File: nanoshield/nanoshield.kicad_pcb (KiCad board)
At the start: 2 copper layers, 73.7 x 55.9 mm, 8 parts, among them J1 Conn_01x20_Socket, J2 Joy, J3 Conn_01x20_Socket, J4 M0S, J5 DIN-5_180degree

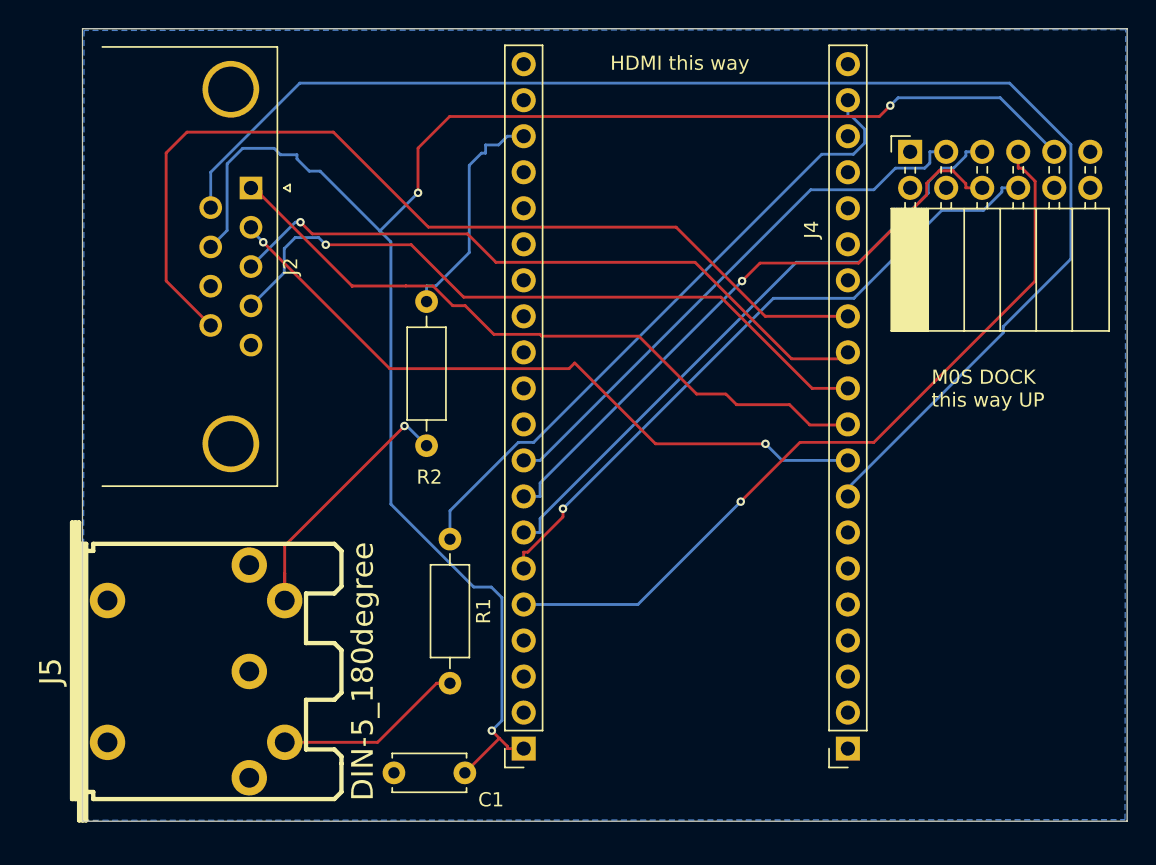
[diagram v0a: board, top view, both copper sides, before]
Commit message: relocation of some components
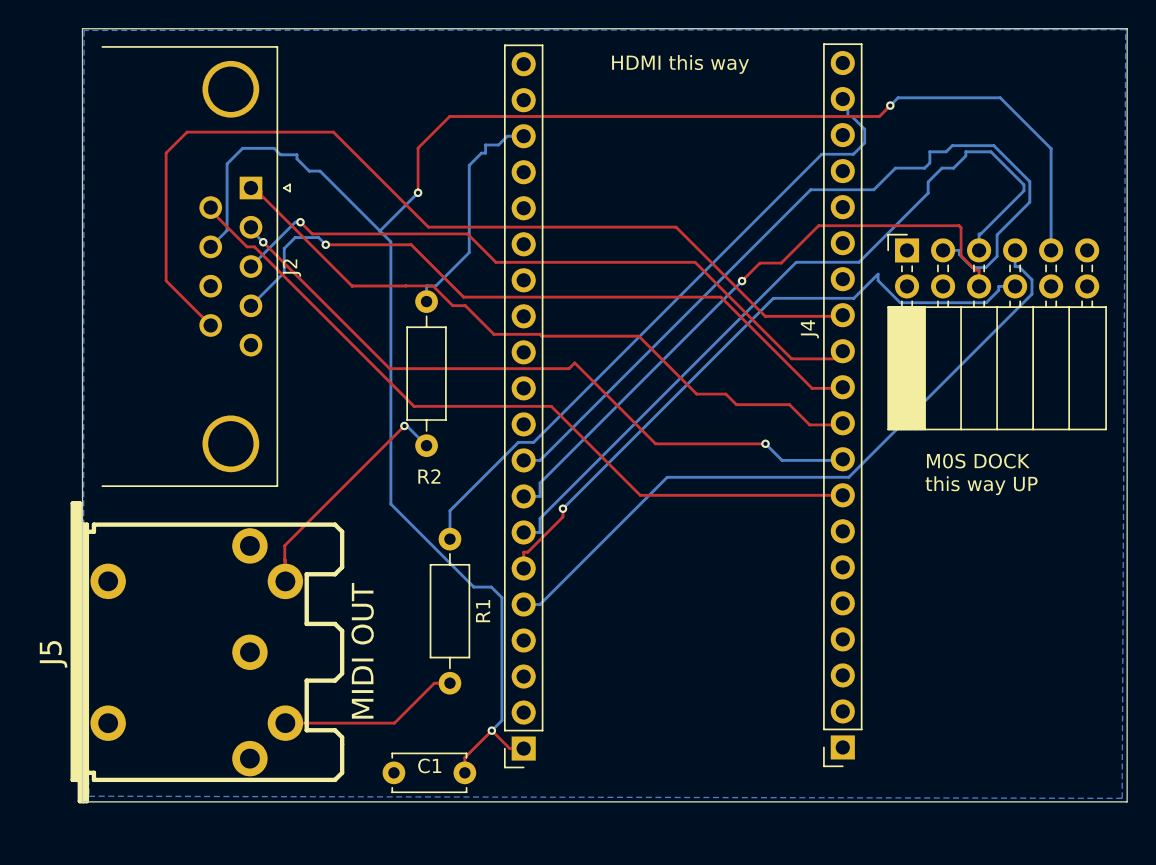
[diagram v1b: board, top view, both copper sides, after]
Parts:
- J5: value DIN-5_180degree -> MIDI OUT
- moved J4 6.95 mm to (149.6, 46.1)
- moved J5 1.35 mm to (100.2, 74.4)
- moved J1 0.37 mm to (145.1, 81.2)
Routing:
- net btn0: track 98.7 -> 52.9 mm
- net irq: track 39.3 -> 57.4 mm
- net csn: track 44.7 -> 54.6 mm
- net +5V: track 121.2 -> 128.2 mm
- net miso: track 55.3 -> 48.6 mm, vias 1 -> 0
- net Net-(J5-Pad5): track 19.1 -> 16.0 mm
- net mosi: track 47.2 -> 46.0 mm
- net left: track 46.9 -> 47.7 mm
- net sck: track 43.5 -> 44.2 mm
- net Net-(J5-Pad4): track 13.4 -> 12.8 mm
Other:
- board size 73.7 x 55.9 mm -> 73.7 x 54.5 mm

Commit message: fix M0S dock location
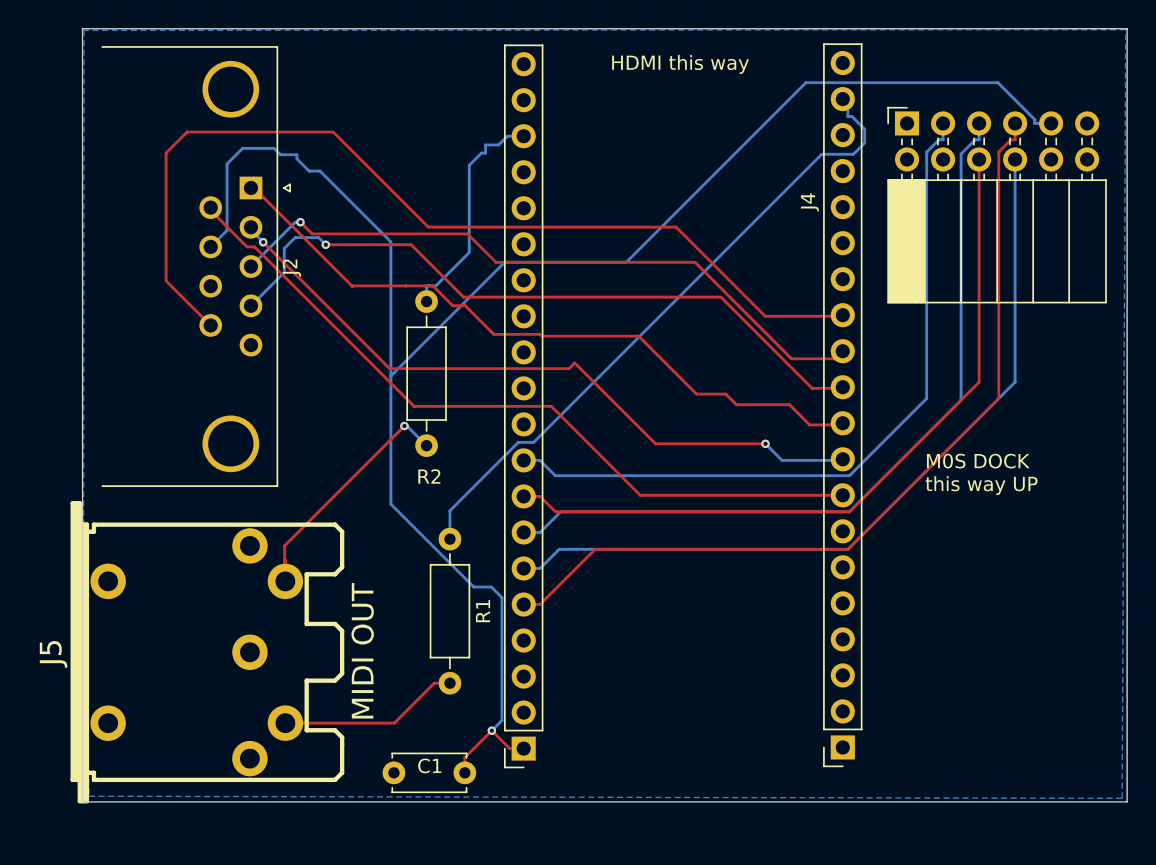
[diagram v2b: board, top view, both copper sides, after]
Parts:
- moved J4 8.95 mm to (149.6, 37.2)
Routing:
- net miso: track 48.6 -> 59.6 mm
- net mosi: track 46.0 -> 55.8 mm, vias 1 -> 0
- net sck: track 44.2 -> 52.0 mm, vias 1 -> 0
- net irq: track 57.4 -> 51.2 mm
- net +5V: track 128.2 -> 123.0 mm, vias 3 -> 1
- net Net-(J5-Pad5): track 16.0 -> 17.3 mm

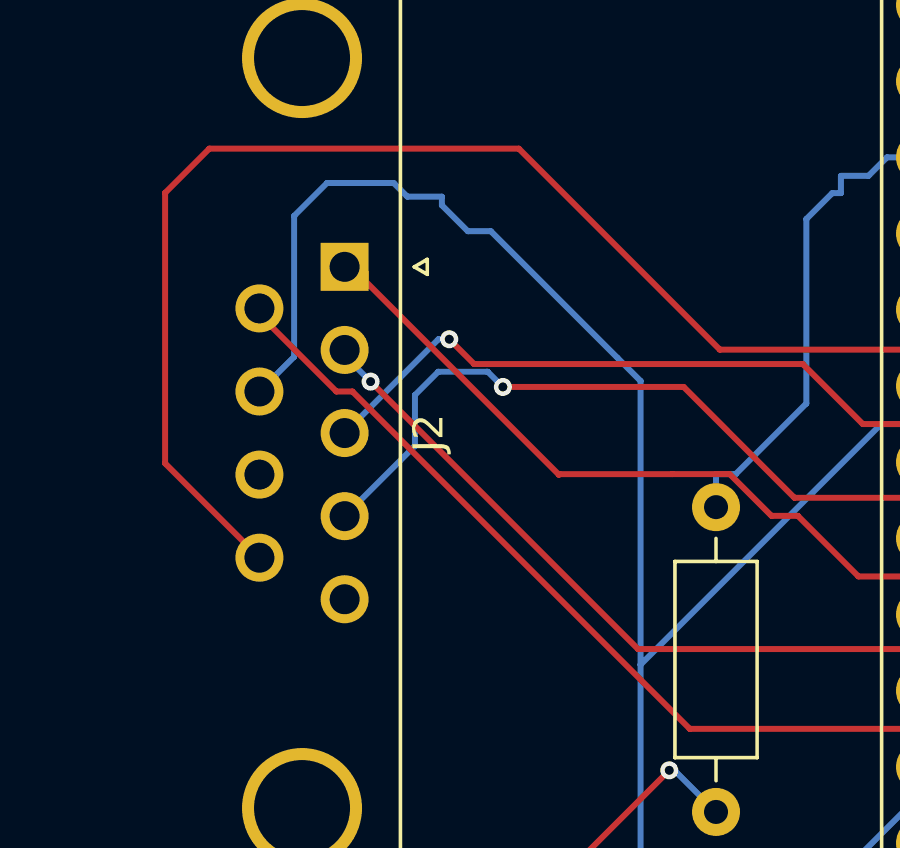
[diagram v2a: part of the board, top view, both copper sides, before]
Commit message: vcc on JOY temp removed
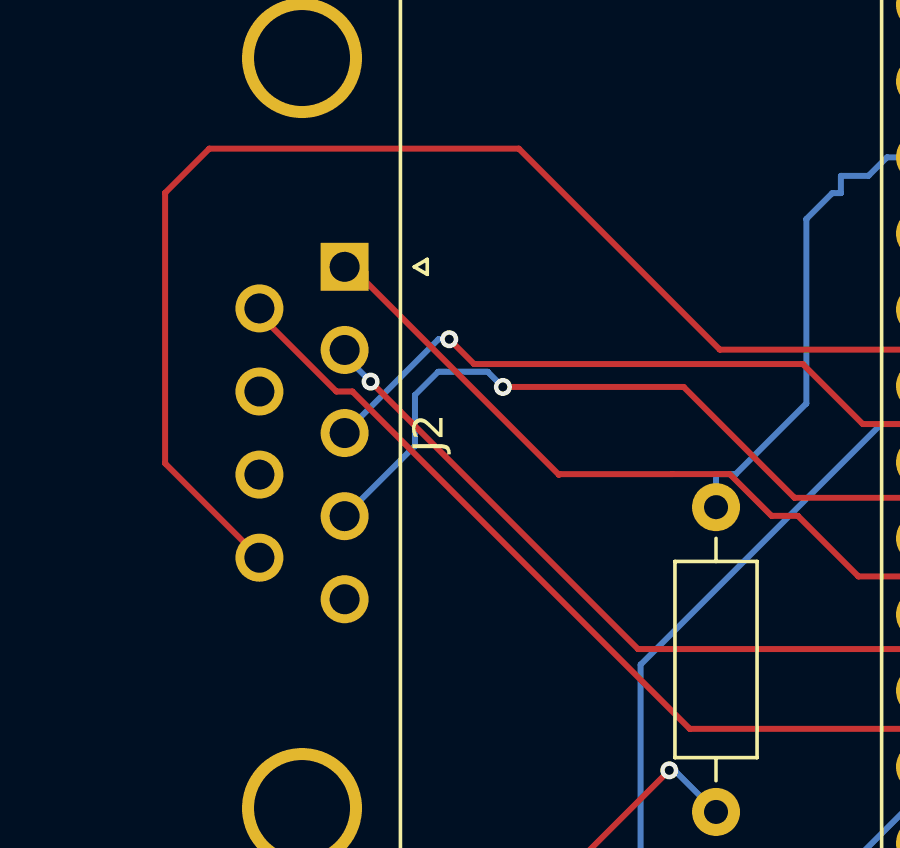
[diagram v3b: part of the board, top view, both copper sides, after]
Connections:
- J2 pad 7: +5V -> unconnected-(J2-Pad7)
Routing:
- net +5V: track 123.0 -> 92.3 mm
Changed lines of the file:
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@@
   (net 47 "unconnected-(J4-Pin_1-Pad1)")
   (net 48 "unconnected-(J4-Pin_2-Pad2)")
+  (net 49 "unconnected-(J2-Pad7)")
   (footprint "Connector_PinSocket_2.54mm:PinSocket_1x20_P2.54mm_Vertical" (layer "F.Cu")
     (at 122.55 81.24 180)
@@
       (net 37 "btn0") (pinfunction "6") (pintype "passive"))
     (pad "7" thru_hole circle (at 4.155 2.84 270) (size 1.6 1.6) (drill 1) (layers "*.Cu" "*.Mask")
-      (net 45 "+5V") (pinfunction "7") (pintype "passive"))
+      (net 49 "unconnected-(J2-Pad7)") (pinfunction "7") (pintype "passive+no_connect"))
     (pad "8" thru_hole circle (at 6.925 2.84 270) (size 1.6 1.6) (drill 1) (layers "*.Cu" "*.Mask")
       (net 28 "GND") (pinfunction "8") (pintype "passive"))
@@
   (segment (start 121.565 81.24) (end 122.55 81.24) (width 0.2) (layer "F.Cu") (net 45))
   (via (at 120.302 79.9768) (size 0.6) (drill 0.3) (layers "F.Cu" "B.Cu") (net 45))
-  (segment (start 101.636 40.0123) (end 102.734 38.915) (width 0.2) (layer "B.Cu") (net 45))
-  (segment (start 113.185 45.5127) (end 113.185 54.9713) (width 0.2) (layer "B.Cu") (net 45))
   (segment (start 121.015 79.2643) (end 120.302 79.9768) (width 0.2) (layer "B.Cu") (net 45))
-  (segment (start 106.562 39.6581) (end 107.426 40.5219) (width 0.2) (layer "B.Cu") (net 45))
   (segment (start 113.185 64.0025) (end 119.032 69.85) (width 0.2) (layer "B.Cu") (net 45))
-  (segment (start 107.426 40.5219) (end 108.194 40.5219) (width 0.2) (layer "B.Cu") (net 45))
   (segment (start 129.7855 46.95) (end 142.4481 34.2874) (width 0.2) (layer "B.Cu") (net 45))
   (segment (start 119.032 69.85) (end 120.271 69.85) (width 0.2) (layer "B.Cu") (net 45))
   (segment (start 142.4481 34.2874) (end 155.984 34.2874) (width 0.2) (layer "B.Cu") (net 45))
-  (segment (start 112.411 44.7389) (end 113.185 45.5127) (width 0.2) (layer "B.Cu") (net 45))
-  (segment (start 102.734 38.915) (end 104.955 38.915) (width 0.2) (layer "B.Cu") (net 45))
   (segment (start 121.015 70.5943) (end 121.015 79.2643) (width 0.2) (layer "B.Cu") (net 45))
   (segment (start 120.271 69.85) (end 121.015 70.5943) (width 0.2) (layer "B.Cu") (net 45))
-  (segment (start 104.955 38.915) (end 105.41 39.37) (width 0.2) (layer "B.Cu") (net 45))
   (segment (start 113.185 54.9713) (end 121.2063 46.95) (width 0.2) (layer "B.Cu") (net 45))
-  (segment (start 105.41 39.37) (end 106.562 39.37) (width 0.2) (layer "B.Cu") (net 45))
   (segment (start 158.5881 36.8915) (end 158.5881 37.16) (width 0.2) (layer "B.Cu") (net 45))
   (segment (start 121.2063 46.95) (end 129.7855 46.95) (width 0.2) (layer "B.Cu") (net 45))
   (segment (start 155.984 34.2874) (end 158.5881 36.8915) (width 0.2) (layer "B.Cu") (net 45))
   (segment (start 159.74 37.16) (end 158.5881 37.16) (width 0.2) (layer "B.Cu") (net 45))
-  (segment (start 106.562 39.37) (end 106.562 39.6581) (width 0.2) (layer "B.Cu") (net 45))
-  (segment (start 101.636 44.7087) (end 101.636 40.0123) (width 0.2) (layer "B.Cu") (net 45))
   (segment (start 113.185 54.9713) (end 113.185 64.0025) (width 0.2) (layer "B.Cu") (net 45))
-  (segment (start 108.194 40.5219) (end 112.411 44.7389) (width 0.2) (layer "B.Cu") (net 45))
-  (segment (start 100.48 45.865) (end 101.636 44.7087) (width 0.2) (layer "B.Cu") (net 45))
   (segment (start 105.699 68.1437) (end 105.7468 68.1915) (width 0.2) (layer "F.Cu") (net 46))
   (segment (start 114.141 58.4921) (end 105.699 66.9337) (width 0.2) (layer "F.Cu") (net 46))

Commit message: fixed distance between headers
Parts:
- moved J1 2.20 mm to (142.8, 81.2)
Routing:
- net btn1: track 67.1 -> 48.1 mm, vias 0 -> 1
- net left: track 47.7 -> 56.6 mm, vias 1 -> 0
- net btn0: track 52.9 -> 57.5 mm
- net +3V3: track 45.6 -> 42.2 mm
- net down: track 48.7 -> 46.3 mm, vias 2 -> 0
- net right: track 49.0 -> 46.9 mm
- net up: track 48.2 -> 47.0 mm
- net Net-(J5-Pad5): track 17.3 -> 16.1 mm
